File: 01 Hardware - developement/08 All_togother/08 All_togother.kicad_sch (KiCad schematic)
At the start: 113 parts, among them IC2 STM32H7A3RIT6TR, J1 POLOLU-2593, J10 Conn_01x03_Pin, J11 Conn_01x03_Pin, J13 ftdi232, J15 ST-link cn3, J16 Boot, J2 ST-link cn6, J3 Conn_01x02_Pin, J4 Conn_01x02_Pin, J5 Conn_01x02_Pin, J6 Conn_01x03_Pin, J7 Conn_01x01_Socket, J8 Conn_01x02_Pin, J9 Conn_01x02_Pin, Q1 BC807, Q2 BC807, SW5 SW_Push_Dual, U1 24C16, U2 LM7805_TO220, X1 8.0MHz 20pF

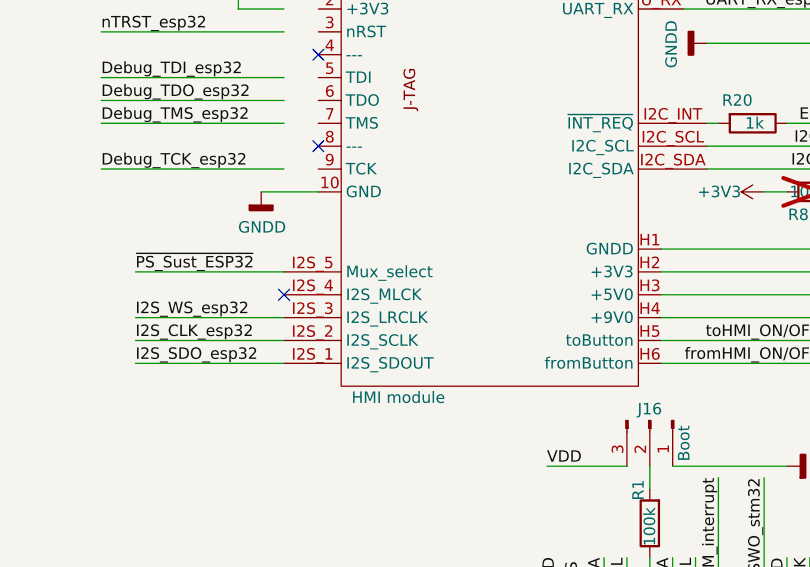
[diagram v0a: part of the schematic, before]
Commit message: hw and esp32 fw inprovements GOLDEN SAMPLE, restore point
- hw - poprawiono footprinty modułów i zamieniono mux select na power supply sustain pin
- fw - poprawiono kalsę StepperOptoPowerOFF
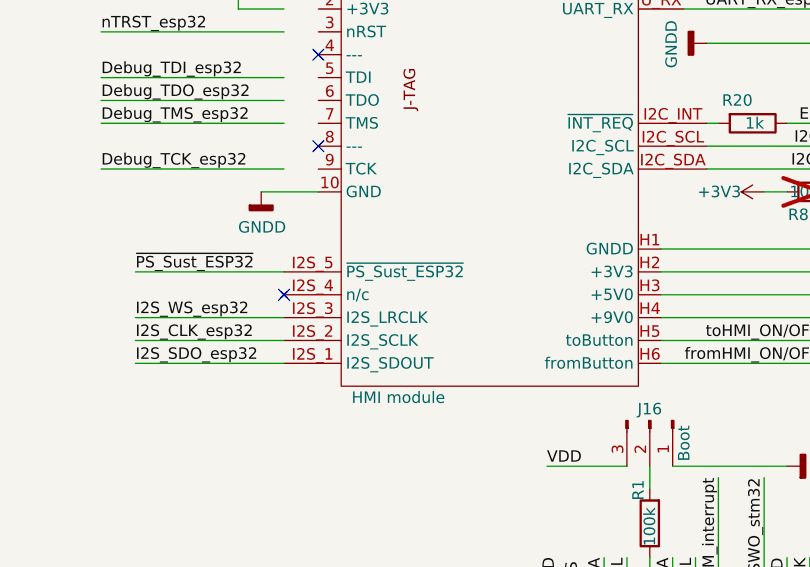
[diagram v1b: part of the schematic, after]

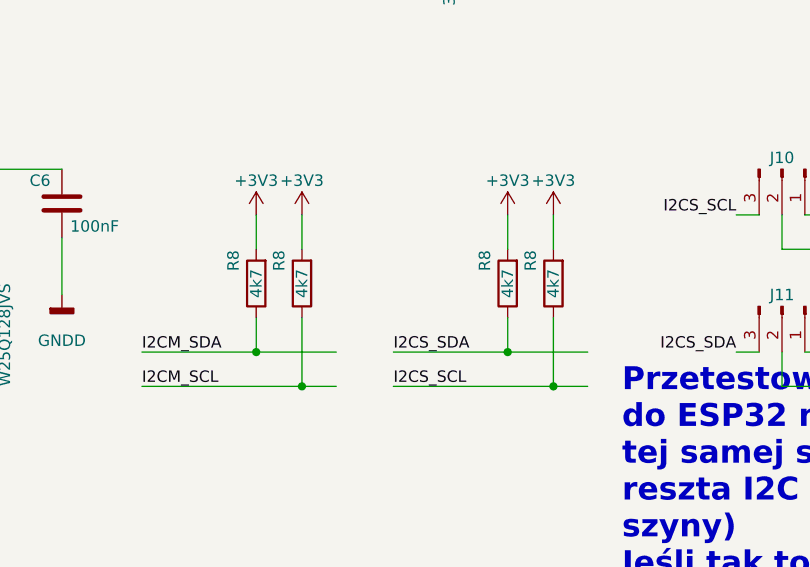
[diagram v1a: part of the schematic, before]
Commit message: stm32 -hw- pull-up resistors 10k
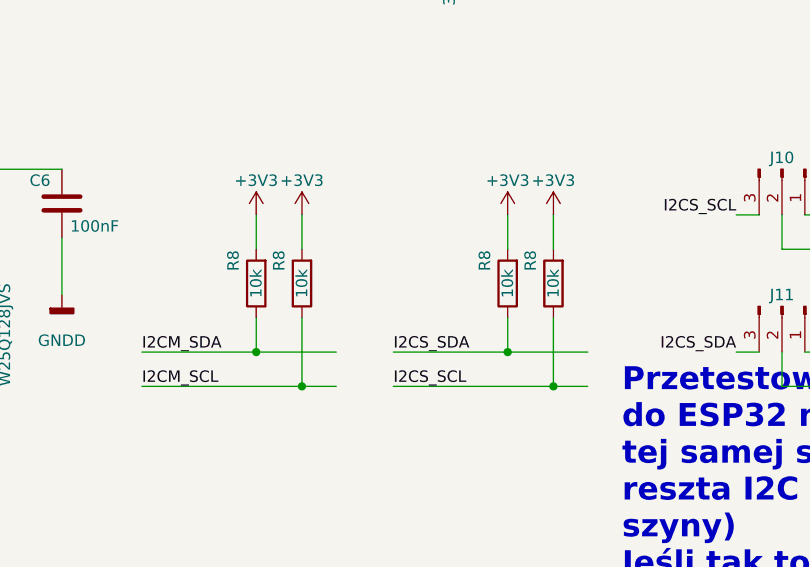
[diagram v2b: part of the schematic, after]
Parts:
- R8: value 4k7 -> 10k; TME no. SMD0603-4K7-1% -> RC0603FR-1310KL
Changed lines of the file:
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@@
       (effects (font (size 1.27 1.27)))
     )
-    (property "Value" "4k7" (at 90.17 182.88 90)
+    (property "Value" "10k" (at 90.17 182.88 90)
       (effects (font (size 1.27 1.27)))
     )
@@
       (effects (font (size 1.27 1.27)) hide)
     )
-    (property "TME no." "SMD0603-4K7-1%" (at 90.17 182.88 0)
+    (property "TME no." "RC0603FR-1310KL" (at 90.17 182.88 0)
       (effects (font (size 1.27 1.27)) hide)
     )
@@
       (effects (font (size 1.27 1.27)))
     )
-    (property "Value" "4k7" (at 123.19 182.88 90)
+    (property "Value" "10k" (at 123.19 182.88 90)
       (effects (font (size 1.27 1.27)))
     )
@@
       (effects (font (size 1.27 1.27)) hide)
     )
-    (property "TME no." "SMD0603-4K7-1%" (at 123.19 182.88 0)
+    (property "TME no." "RC0603FR-1310KL" (at 123.19 182.88 0)
       (effects (font (size 1.27 1.27)) hide)
     )
@@
       (effects (font (size 1.27 1.27)))
     )
-    (property "Value" "4k7" (at 118.11 182.88 90)
+    (property "Value" "10k" (at 118.11 182.88 90)
       (effects (font (size 1.27 1.27)))
     )
@@
       (effects (font (size 1.27 1.27)) hide)
     )
-    (property "TME no." "SMD0603-4K7-1%" (at 118.11 182.88 0)
+    (property "TME no." "RC0603FR-1310KL" (at 118.11 182.88 0)
       (effects (font (size 1.27 1.27)) hide)
     )
@@
       (effects (font (size 1.27 1.27)))
     )
-    (property "Value" "4k7" (at 95.25 182.88 90)
+    (property "Value" "10k" (at 95.25 182.88 90)
       (effects (font (size 1.27 1.27)))
     )
@@
       (effects (font (size 1.27 1.27)) hide)
     )
-    (property "TME no." "SMD0603-4K7-1%" (at 95.25 182.88 0)
+    (property "TME no." "RC0603FR-1310KL" (at 95.25 182.88 0)
       (effects (font (size 1.27 1.27)) hide)
     )

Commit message: all toogothert -hw- poprawiono crystal
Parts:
- C9: value 30pF -> 30pF n.a.; now not fitted
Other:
- note added: "C10 i C11 są niepotrzebne przy tym krysztale. Wylutować je z PCB"
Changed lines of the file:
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@@
     (effects (font (face "Arial Narrow") (size 2.54 2.54) (thickness 0.508) bold (color 255 0 21 1)) (justify left top))
   )
+  (text "C10 i C11 są niepotrzebne\nprzy tym krysztale.\nWylutować je z PCB"
+    (at 116.84 113.03 0)
+    (effects (font (size 2.5 2.5) (color 255 0 34 1)) (justify left bottom))
+  )
   (text "Sprawdzić czy na\nwejściu są\nkondensatory" (at 407.67 92.71 0)
     (effects (font (size 5 5) bold (color 255 0 11 1)) (justify left bottom))
@@
   )
   (symbol (lib_id "Device:C") (at 110.49 144.78 90) (mirror x) (unit 1)
-    (in_bom yes) (on_board yes) (dnp no)
+    (in_bom yes) (on_board yes) (dnp yes)
     (property "Reference" "C9" (at 109.3216 147.701 0)
       (effects (font (size 1.27 1.27)) (justify left))
     )
-    (property "Value" "30pF" (at 111.633 147.701 0)
+    (property "Value" "30pF n.a." (at 111.633 147.701 0)
       (effects (font (size 1.27 1.27)) (justify left))
     )
@@
   )
   (symbol (lib_id "Device:C") (at 110.49 118.11 270) (mirror x) (unit 1)
-    (in_bom yes) (on_board yes) (dnp no)
+    (in_bom yes) (on_board yes) (dnp yes)
     (property "Reference" "C9" (at 111.6584 115.189 0)
       (effects (font (size 1.27 1.27)) (justify left))
     )
-    (property "Value" "30pF" (at 109.347 115.189 0)
+    (property "Value" "30pF n.a." (at 109.347 115.189 0)
       (effects (font (size 1.27 1.27)) (justify left))
     )

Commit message: dodano ERRATY
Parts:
- renumbered C6 to C1, C9 to C10, C9 to C11, C6 to C12, C23 to C13, C6 to C14, C6 to C15, C6 to C16, C6 to C17, C6 to C18, C6 to C19, C6 to C2, C16 to C20, C16 to C21, C6 to C22, C6 to C23, C6 to C3, C6 to C4, C6 to C5, C6 to C7, C6 to C8, C23 to C9, D4 to D10, D4 to D11, D4 to D3, D4 to D5, D4 to D6, D4 to D7, D4 to D8, D4 to D9, R8 to R12, R8 to R13, R8 to R16, R8 to R17, R8 to R18, R8 to R19, R2 to R25, R2 to R26, R2 to R27, R2 to R28, R2 to R29, R2 to R30, R2 to R31, R8 to R5, R8 to R6, R8 to R7, SW5 to SW1
